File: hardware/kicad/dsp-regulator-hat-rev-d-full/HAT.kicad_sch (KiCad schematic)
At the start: 62 parts, among them J10 USB Hub I2C, J11 SWD_Debug_Header, J12 FW-10-05-X-D-XXX-XXX-A, J13 Conn_01x01_Pin, J14 Conn_01x01_Pin, J15 Conn_01x01_Pin, J17 SWD_Debug_Header, J18 FW-10-05-X-D-XXX-XXX-A, J19 20021121-00010C4LF, J7 Fan Control, J8 Connector, USB-TYPE-C-16P, J9 Display Uart, Q9 AO3400A, U12 W25Q128, U13 AHT20_C2757850, U15 AMS1117-3.3, U16 CH340C

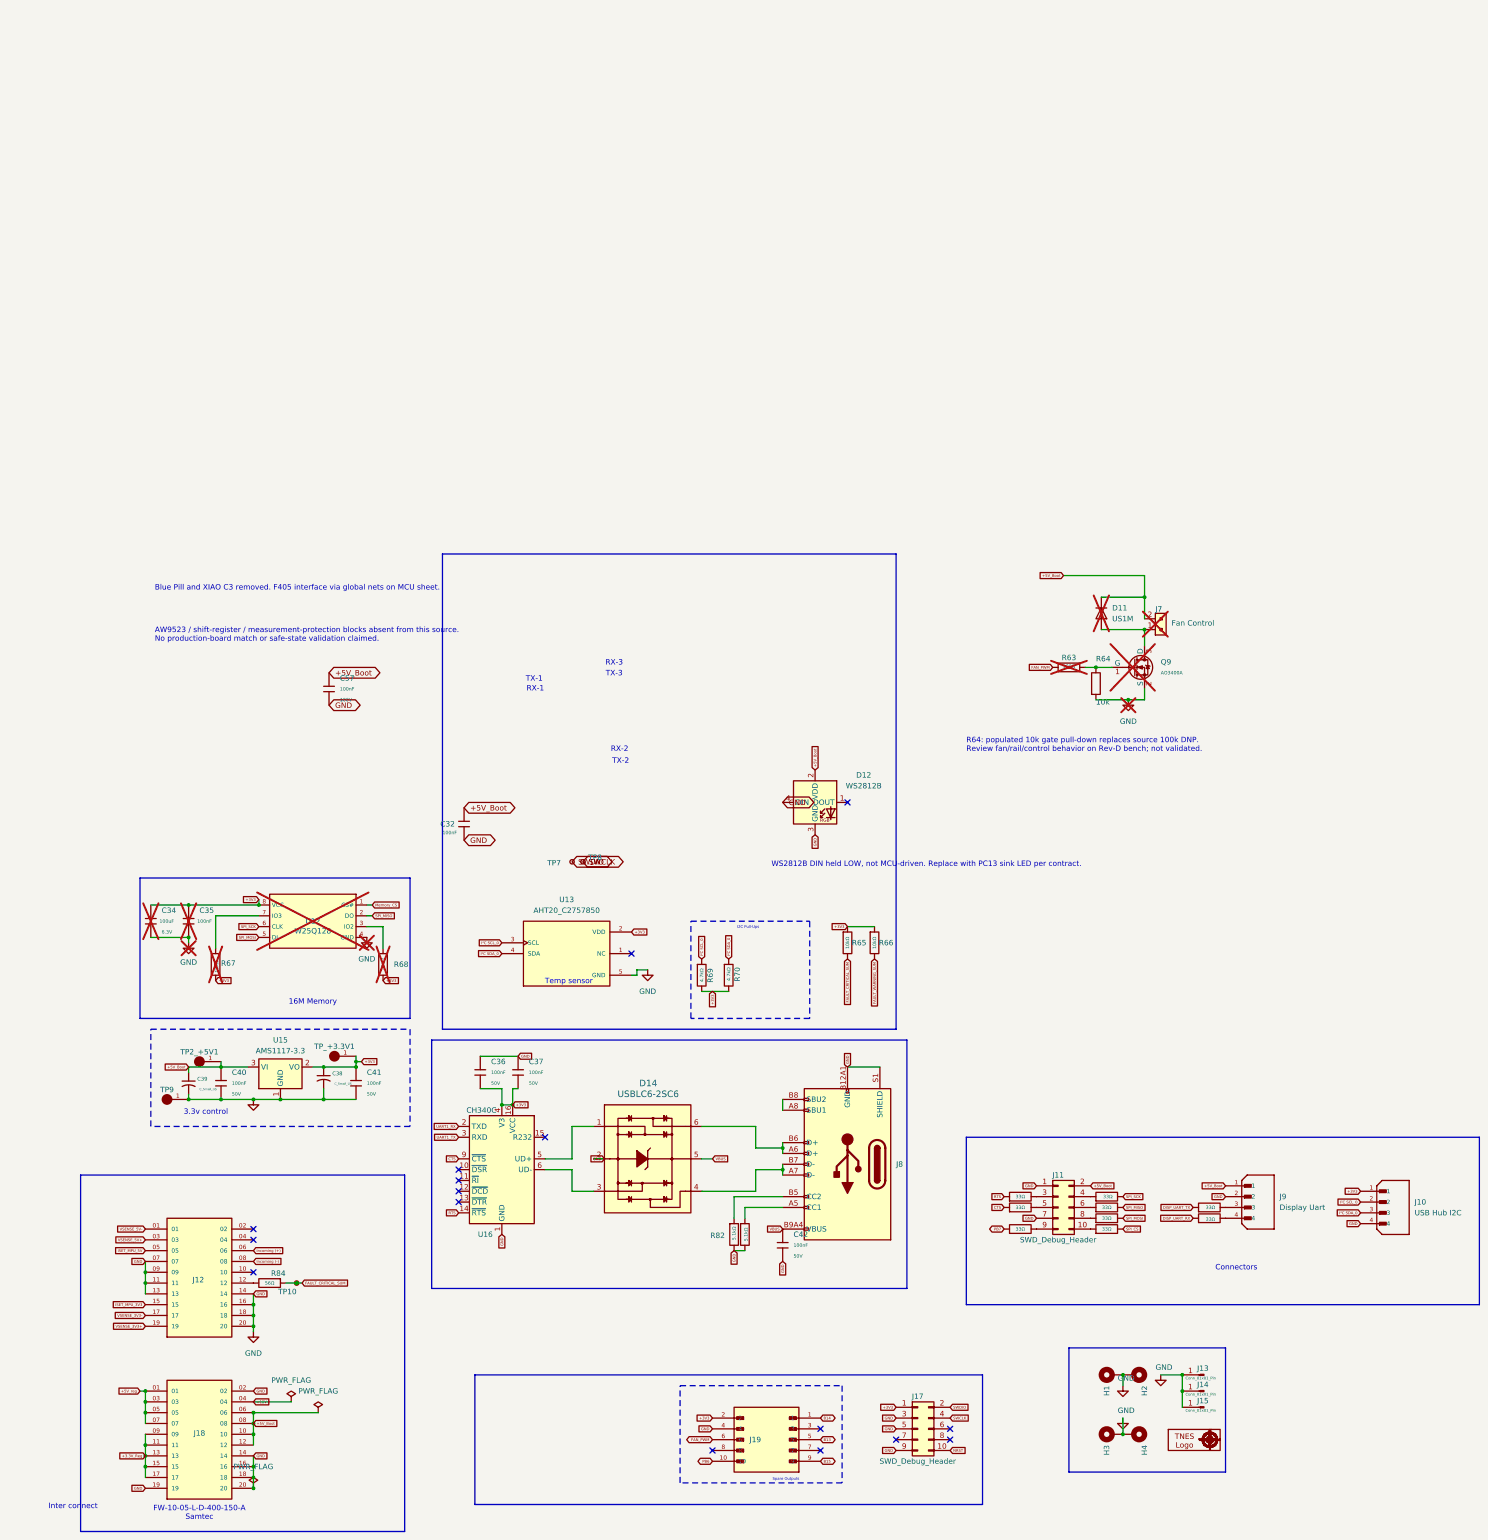
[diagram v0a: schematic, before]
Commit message: hw(hat): rebuild partial Rev-D HAT from selected Rev-C schematic (#111)
* docs(hat): record Rev-C production source mismatch

Co-authored-by: Copilot App <223556219+Copilot@users.noreply.github.com>

* docs(hat): mark source mismatch non-blocking

Co-authored-by: Copilot App <223556219+Copilot@users.noreply.github.com>

* docs(hat): defer fan check and session 5

Co-authored-by: Copilot App <223556219+Copilot@users.noreply.github.com>

* fix(hat): rebuild Rev-D from selected production schematic

Replace the incorrect repository-derived HAT baseline with the user-selected production-folder schematic; preserve source circuits and document unsupported interfaces.

Co-authored-by: Copilot App <223556219+Copilot@users.noreply.github.com>

---------

Co-authored-by: Copilot App <223556219+Copilot@users.noreply.github.com>
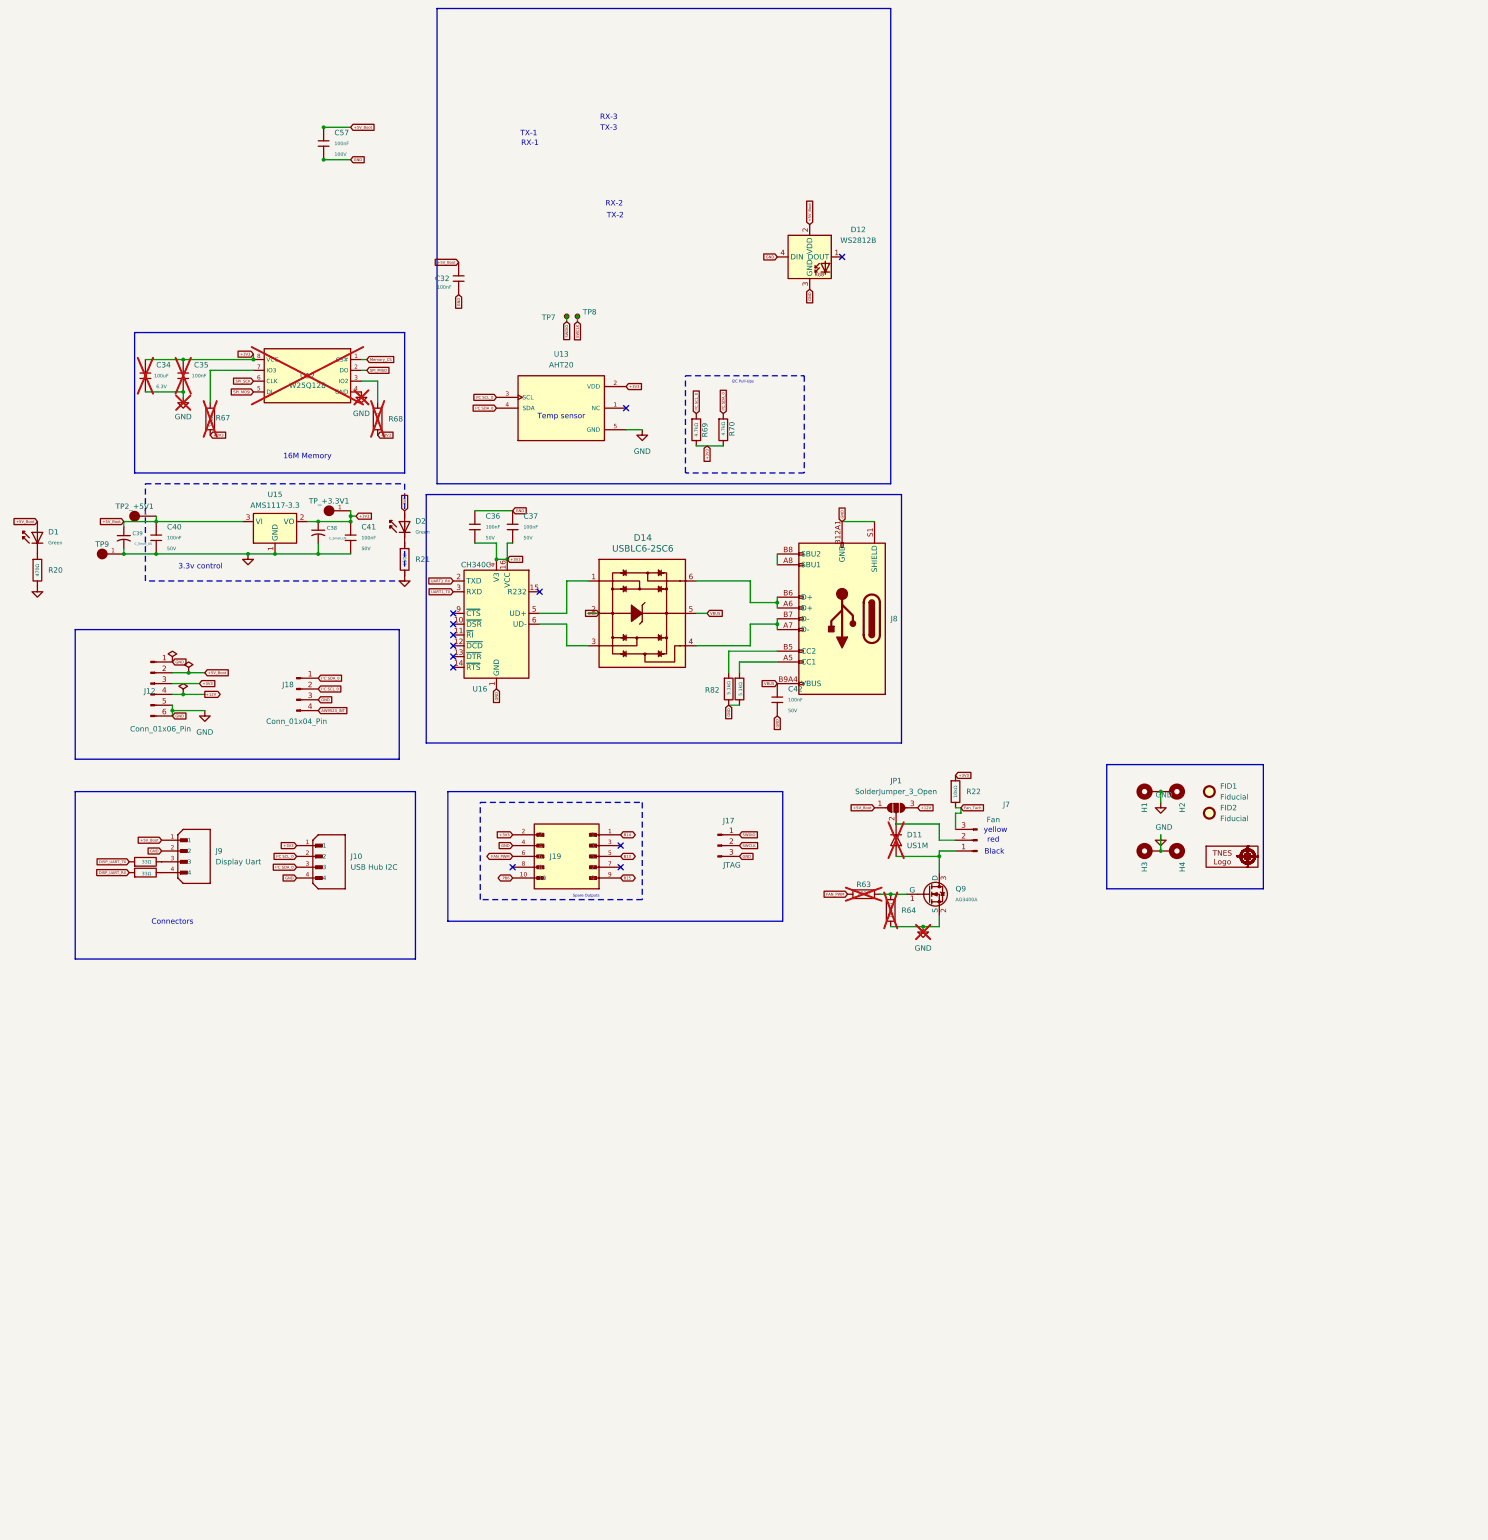
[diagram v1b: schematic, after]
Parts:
- removed J11: SWD_Debug_Header, Connector_IDC:IDC-Header_2x05_P2.54mm_Vertical, symbol Connector_Generic:Conn_02x05_Odd_Even
- removed J13, J14, J15: Conn_01x01_Pin, Connector_Wire:SolderWire-1sqmm_1x01_D1.4mm_OD2.7mm, symbol Connector:Conn_01x01_Pin
- removed R65, R66: 10kΩ, PCM_JLCPCB:R_0805, symbol PCM_JLCPCB-Resistors:0805,10kΩ
- removed R73, R74, R75, R76, R78, R80, R81: 33Ω, PCM_JLCPCB:R_0805, symbol PCM_JLCPCB-Resistors:0805,33Ω
- removed R84: 56Ω, PCM_JLCPCB:R_0805, symbol PCM_JLCPCB-Resistors:0805,56Ω
- removed TP10: TestPoint_Small, Connector_PinHeader_1.00mm:PinHeader_1x01_P1.00mm_Vertical, symbol Connector:TestPoint_Small
- added D1, D2: Green, PCM_JLCPCB:D_0805, symbol PCM_JLCPCB-Diodes:LED,0805,Green
- added FID1, FID2: Fiducial, Fiducial:Fiducial_0.75mm_Mask1.5mm, symbol Mechanical:Fiducial
- added JP1: SolderJumper_3_Open, Jumper:SolderJumper-3_P1.3mm_Open_RoundedPad1.0x1.5mm, symbol Jumper:SolderJumper_3_Open
- added R20: 470Ω, PCM_JLCPCB:R_0805, symbol PCM_JLCPCB-Resistors:0805,470Ω
- added R21: 150Ω, PCM_JLCPCB:R_0805, symbol PCM_JLCPCB-Resistors:0805,150Ω
- added R22: 10kΩ, PCM_JLCPCB:R_0805, symbol PCM_JLCPCB-Resistors:0805,10kΩ
- J10, J9: LCSC C144394 -> C144395
- J12: value FW-10-05-X-D-XXX-XXX-A -> Conn_01x06_Pin; footprint 1My_Parts_ Connectors:SAMTEC_FW-10-05-X-D-XXX-XXX-A -> Connector_PinHeader_2.54mm:PinHeader_1x06_P2.54mm_Vertical; symbol 1My_Connectors:FW-10-05-X-D-XXX-XXX-A -> Connector:Conn_01x06_Pin; AVAILABILITY Not in stock -> (none); LCSC (none) -> C492414; MF Samtec -> (none); MP FW-10-05-G-D-300-300-A -> (none); PACKAGE None -> (none); PRICE None -> (none)
- J17: value SWD_Debug_Header -> JTAG; footprint Connector_IDC:IDC-Header_2x05_P2.54mm_Vertical -> Connector_PinHeader_2.54mm:PinHeader_1x03_P2.54mm_Vertical_SMD_Pin1Right; symbol Connector_Generic:Conn_02x05_Odd_Even -> Connector:Conn_01x03_Pin
- J18: value FW-10-05-X-D-XXX-XXX-A -> Conn_01x04_Pin; footprint 1My_Parts_ Connectors:SAMTEC_FW-10-05-X-D-XXX-XXX-A -> Connector_PinHeader_2.54mm:PinHeader_1x04_P2.54mm_Vertical; symbol 1My_Connectors:FW-10-05-X-D-XXX-XXX-A -> Connector:Conn_01x04_Pin; AVAILABILITY Not in stock -> (none); LCSC (none) -> C492412; MF Samtec -> (none); MP FW-10-05-G-D-300-300-A -> (none); PACKAGE None -> (none); PRICE None -> (none)
- J7: value Fan Control -> Fan; footprint digikey-footprints:PinHeader_1x2_P2.5mm_Drill1.1mm -> Connector_PinHeader_2.54mm:PinHeader_1x03_P2.54mm_Vertical; symbol dk_Rectangular-Connectors-Headers-Male-Pins:B2B-XH-A_LF__SN_ -> Connector:Conn_01x03_Pin; Category Connectors, Interconnects -> (none); DK_Datasheet_Link http://www.jst-mfg.com/product/pdf/eng/eXH.pdf -> (none); DK_Detail_Page /product-detail/en/jst-sales-america-inc/B2B-XH-A(LF)(SN)/4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 -> (none); Description_1 CONN HEADER VERT 2POS 2.5MM -> (none); Digi-Key_PN 455-2247-ND -> (none); Family Rectangular Connectors - Headers, Male Pins -> (none); LCSC C158012 -> C29275; MPN B2B-XH-A(LF)(SN) -> (none); Manufacturer JST Sales America Inc. -> (none); Status Active -> (none); now fitted
- Q9: now fitted
- R64: value 10k -> 100kΩ; footprint Resistor_SMD:R_0805_2012Metric -> PCM_JLCPCB:R_0805; symbol Device:R -> PCM_JLCPCB-Resistors:0805,100kΩ; Attrition Qty (none) -> 10; Category (none) -> Resistors,Chip Resistor - Surface Mount; Class (none) -> Basic Component; LCSC (none) -> C149504; Manufacturer (none) -> UNI-ROYAL(Uniroyal Elec); Minimum Qty (none) -> 20; Operating Temperature Range (none) -> -55°C~+155°C; Overload Voltage (Max) (none) -> 150V; Part (none) -> 0805W8F1003T5E; Power(Watts) (none) -> 125mW; Price (none) -> 0.005USD; Process (none) -> SMT; Resistance (none) -> 100kΩ; Stock (none) -> 3946237; Temperature Coefficient (none) -> ±100ppm/°C; Tolerance (none) -> ±1%; Type (none) -> Thick Film Resistors; now not fitted
- U13: value AHT20_C2757850 -> AHT20; footprint Package_SON:WSON-6-1EP_3x3mm_P0.95mm -> 1My_Parts_ ICs:Humidity sensor
- U16: LCSC C14267 -> C84681
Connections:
- net +12V: now also J12.4 (Pin_4), JP1.3 (B); no longer J18.04
- net +3V3: now also J12.3 (Pin_3), D2.2, R22.1; no longer J17.1 (Pin_1)
- net +5V_Boot: now also J12.2 (Pin_2), D1.2, JP1.1 (A); no longer D11.1 (K), J18.06, J18.08, J18.10, J18.12, J7.2
- net GND: now also J12.1 (Pin_1), J12.5 (Pin_5), J12.6 (Pin_6), J18.3 (Pin_3), R20.2, R21.2; no longer J12.07, J12.09, J12.11, J12.13, J12.14, J12.16, J12.18, J12.20, J17.5 (Pin_5), J17.9 (Pin_9), J18.02, J18.14, J18.16, J18.18, J18.19, J18.20
- net I²C SCL_0: now also J18.2 (Pin_2)
- net I²C SDA_0: now also J18.1 (Pin_1)
- net SWCLK: now also J17.2 (Pin_2); no longer J17.4 (Pin_4)
- net SWDIO: now also J17.1 (Pin_1); no longer J17.2 (Pin_2)
- removed net +3.3V_Reg: J18.09, J18.11, J18.13, J18.15, J18.17
- removed net +5V_reg: J18.01, J18.03, J18.05, J18.07
- net CTS: no longer names the net of U16.9 (~{CTS})
- removed net ISET_MPU_3V3: J12.15
- removed net ISET_MPU_5V: J12.05
- removed net Incoming (+): J12.06
- removed net Incoming (-): J12.08
- removed net NRST: J17.10 (Pin_10)
- net RTS: no longer names the net of U16.14 (~{RTS})
- removed net VSENSE_3V3+: J12.19
- removed net VSENSE_3V3-: J12.17
- removed net VSENSE_5V+: J12.03
- removed net VSENSE_5V-: J12.01
- new net: D11.1 (K), J7.2 (Pin_2), JP1.2 (C)
- new net: D1.1, R20.1
- new net: D2.1, R21.1
- new net AW9523_INT: J18.4 (Pin_4)
- new net Fan_Tach: J7.3 (Pin_3), R22.2
- no-connect marks 16 -> 12
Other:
- note added: "Black"
- note added: "red"
- note added: "yellow"
- note removed: "AW9523 / shift-register / measurement-protection blocks absent from this source. No production-board match or safe-state validation claimed."
- note removed: "Blue Pill and XIAO C3 removed. F405 interface via global nets on MCU sheet."
- note removed: "FW-10-05-L-D-400-150-A Samtec"
- note removed: "Inter connect"
- note removed: "R64: populated 10k gate pull-down replaces source 100k DNP. Review fan/rail/control behavior on Rev-D bench; not validated."
- note removed: "WS2812B DIN held LOW, not MCU-driven. Replace with PC13 sink LED per contract."
- title: Rev-D HAT Reuse Candidates - Initial Integration -> DSP Regulator HAT Rev-D - selected Rev-C reuse
- moved on the sheet: C32, C34, C35, C36, C37, C38, C39, C40, C41, C42, C57, D11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
